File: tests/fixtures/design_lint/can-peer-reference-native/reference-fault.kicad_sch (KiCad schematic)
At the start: 4 parts, among them U1 Synthetic CAN transceiver, U2 Synthetic CAN transceiver, U3 Synthetic CAN transceiver

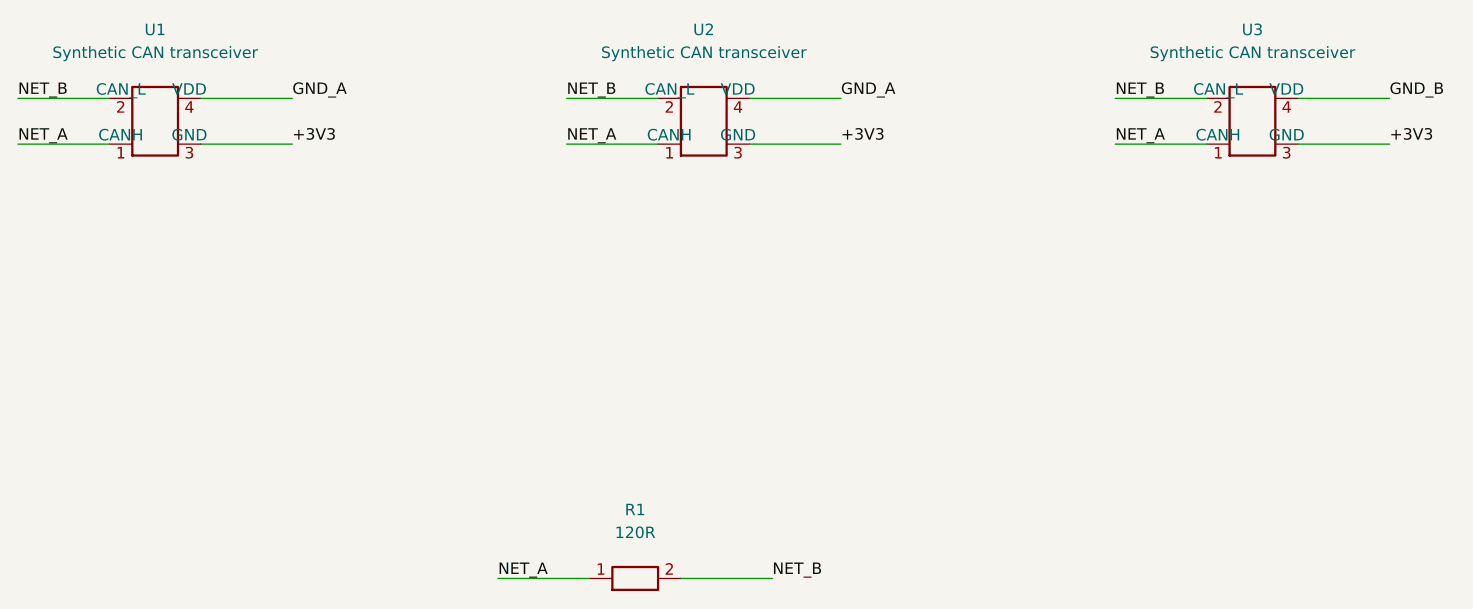
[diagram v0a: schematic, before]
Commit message: Correct CAN reference native fixture wiring
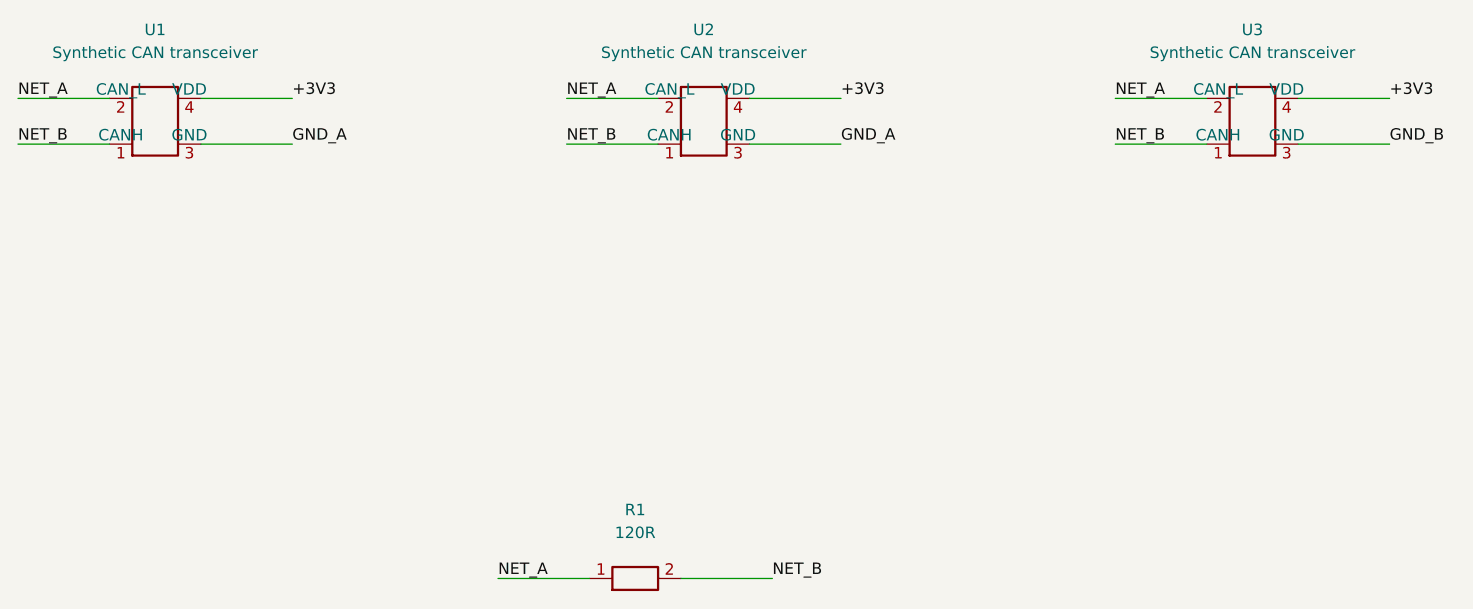
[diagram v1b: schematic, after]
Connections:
- net +3V3: now also U1.4 (VDD), U2.4 (VDD), U3.4 (VDD); no longer U1.3 (GND), U2.3 (GND), U3.3 (GND)
- net GND_A: now also U1.3 (GND), U2.3 (GND); no longer U1.4 (VDD), U2.4 (VDD)
- net GND_B: now also U3.3 (GND); no longer U3.4 (VDD)
- net NET_A: now also U1.2 (CAN_L), U2.2 (CAN_L), U3.2 (CAN_L); no longer U1.1 (CANH), U2.1 (CANH), U3.1 (CANH)
- net NET_B: now also U1.1 (CANH), U2.1 (CANH), U3.1 (CANH); no longer U1.2 (CAN_L), U2.2 (CAN_L), U3.2 (CAN_L)
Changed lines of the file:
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@@
     (stroke (width 0) (type default))
 )
-  (label "NET_B" (at 60.96 73.66 0)
+  (label "NET_A" (at 60.96 73.66 0)
     (effects (font (size 1.27 1.27)) (justify left bottom))
 )
@@
     (stroke (width 0) (type default))
 )
-  (label "NET_A" (at 60.96 78.74 0)
+  (label "NET_B" (at 60.96 78.74 0)
     (effects (font (size 1.27 1.27)) (justify left bottom))
 )
@@
     (stroke (width 0) (type default))
 )
-  (label "NET_B" (at 121.92 73.66 0)
+  (label "NET_A" (at 121.92 73.66 0)
     (effects (font (size 1.27 1.27)) (justify left bottom))
 )
@@
     (stroke (width 0) (type default))
 )
-  (label "NET_A" (at 121.92 78.74 0)
+  (label "NET_B" (at 121.92 78.74 0)
     (effects (font (size 1.27 1.27)) (justify left bottom))
 )
@@
     (stroke (width 0) (type default))
 )
-  (label "NET_B" (at 182.88 73.66 0)
+  (label "NET_A" (at 182.88 73.66 0)
     (effects (font (size 1.27 1.27)) (justify left bottom))
 )
@@
     (stroke (width 0) (type default))
 )
-  (label "NET_A" (at 182.88 78.74 0)
+  (label "NET_B" (at 182.88 78.74 0)
     (effects (font (size 1.27 1.27)) (justify left bottom))
 )
@@
     (stroke (width 0) (type default))
 )
-  (label "GND_A" (at 91.44 73.66 0)
+  (label "+3V3" (at 91.44 73.66 0)
     (effects (font (size 1.27 1.27)) (justify left bottom))
 )
@@
     (stroke (width 0) (type default))
 )
-  (label "+3V3" (at 91.44 78.74 0)
+  (label "GND_A" (at 91.44 78.74 0)
     (effects (font (size 1.27 1.27)) (justify left bottom))
 )
@@
     (stroke (width 0) (type default))
 )
-  (label "GND_A" (at 152.40 73.66 0)
+  (label "+3V3" (at 152.40 73.66 0)
     (effects (font (size 1.27 1.27)) (justify left bottom))
 )
@@
     (stroke (width 0) (type default))
 )
-  (label "+3V3" (at 152.40 78.74 0)
+  (label "GND_A" (at 152.40 78.74 0)
     (effects (font (size 1.27 1.27)) (justify left bottom))
 )
@@
     (stroke (width 0) (type default))
 )
-  (label "GND_B" (at 213.36 73.66 0)
+  (label "+3V3" (at 213.36 73.66 0)
     (effects (font (size 1.27 1.27)) (justify left bottom))
 )
@@
     (stroke (width 0) (type default))
 )
-  (label "+3V3" (at 213.36 78.74 0)
+  (label "GND_B" (at 213.36 78.74 0)
     (effects (font (size 1.27 1.27)) (justify left bottom))
 )
